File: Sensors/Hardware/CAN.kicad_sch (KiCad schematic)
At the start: 9 parts, among them U13 SN65HVD230

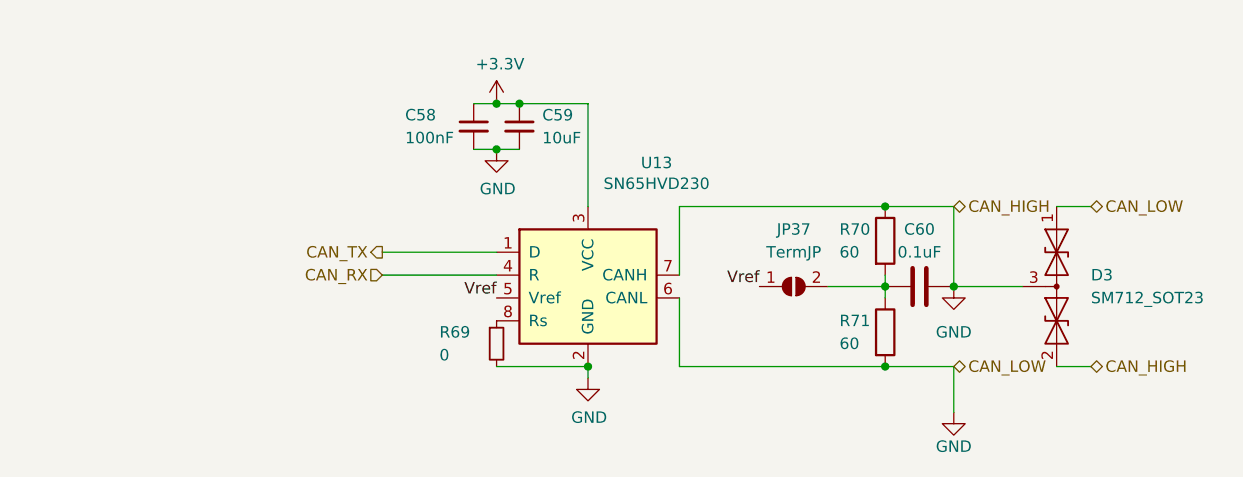
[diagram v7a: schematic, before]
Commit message: fixed the CAN
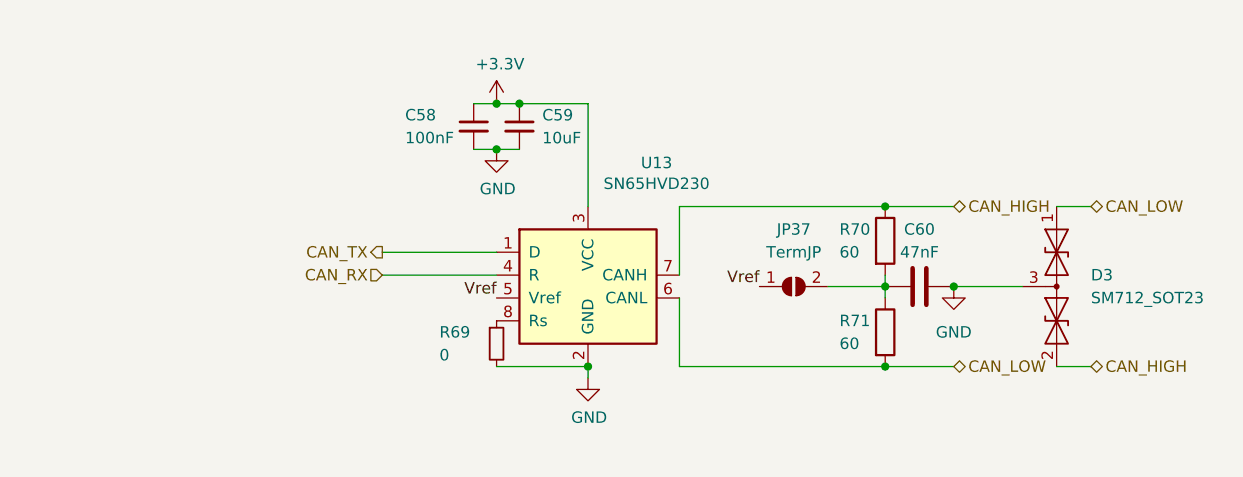
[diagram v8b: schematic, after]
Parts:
- C60: value 0.1uF -> 47nF
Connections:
- net GND: no longer D3.1 (A1), D3.2 (A2), R70.1, R71.2, U13.6 (CANL), U13.7 (CANH)
- new net CAN_HIGH: D3.2 (A2), R70.1, U13.7 (CANH)
- new net CAN_LOW: D3.1 (A1), R71.2, U13.6 (CANL)
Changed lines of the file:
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@@
-    (stroke (width 0) (type default))
-  )
-  (wire (pts (xy 175.26 80.01) (xy 175.26 88.9))
     (stroke (width 0) (type default))
   )
@@
   )
   (wire (pts (xy 111.76 87.63) (xy 124.46 87.63))
-    (stroke (width 0) (type default))
-  )
-  (wire (pts (xy 175.26 97.79) (xy 175.26 102.87))
     (stroke (width 0) (type default))
   )
@@
     )
   )
-  (symbol (lib_id "power:GND") (at 175.26 102.87 0) (unit 1)
-    (in_bom yes) (on_board yes) (dnp no) (fields_autoplaced)
-    (property "Reference" "#PWR0156" (at 175.26 109.22 0)
-      (effects (font (size 1.27 1.27)) hide)
-    )
-    (property "Value" "GND" (at 175.26 106.68 0)
-      (effects (font (size 1.27 1.27)))
-    )
-    (property "Footprint" "" (at 175.26 102.87 0)
-      (effects (font (size 1.27 1.27)) hide)
-    )
-    (property "Datasheet" "" (at 175.26 102.87 0)
-      (effects (font (size 1.27 1.27)) hide)
-    )
-    (pin "1")
-    (instances
-      (project "sensorboard"
-        (path "/26801cfb-b53b-4a6a-a2f4-5f4986565765/f5d08e6e-78a9-4643-8dbf-1f1240e72106"
-          (reference "#PWR0156") (unit 1)
-        )
-      )
-    )
-  )
   (symbol (lib_id "Device:C_Small") (at 121.92 71.12 0) (unit 1)
     (in_bom yes) (on_board yes) (dnp no) (fields_autoplaced)
@@
       (effects (font (size 1.27 1.27)))
     )
-    (property "Value" "0.1uF" (at 171.45 85.09 90)
-      (effects (font (size 1.27 1.27)))
-    )
+    (property "Value" "47nF" (at 171.45 85.09 90)
+      (effects (font (size 1.27 1.27)))
+    )
